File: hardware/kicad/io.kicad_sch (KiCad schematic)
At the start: 18 parts, among them J12 Conn_01x08, J15 Conn_01x02, J18 Conn_01x07, J4 UART_A, J5 UART_B, J6 Port_A, J7 Port_B, U11 74AC138, U12 SC16C752, U13 W65C22S

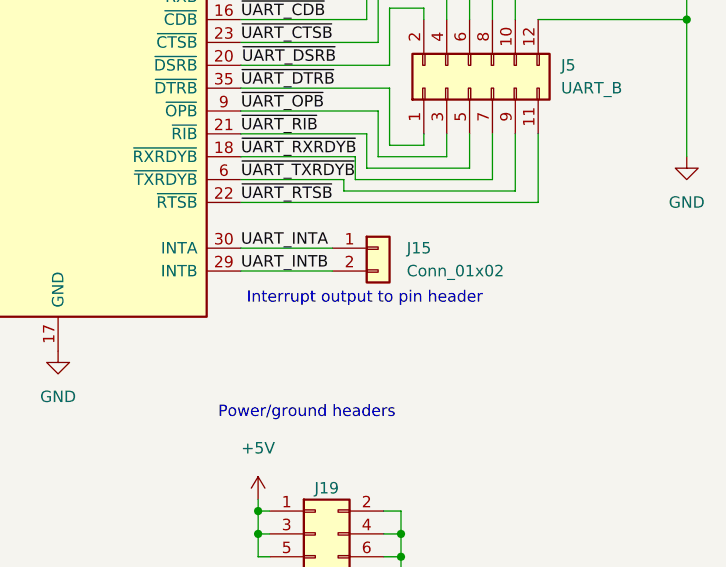
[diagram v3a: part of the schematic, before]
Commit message: add gerbers for test board
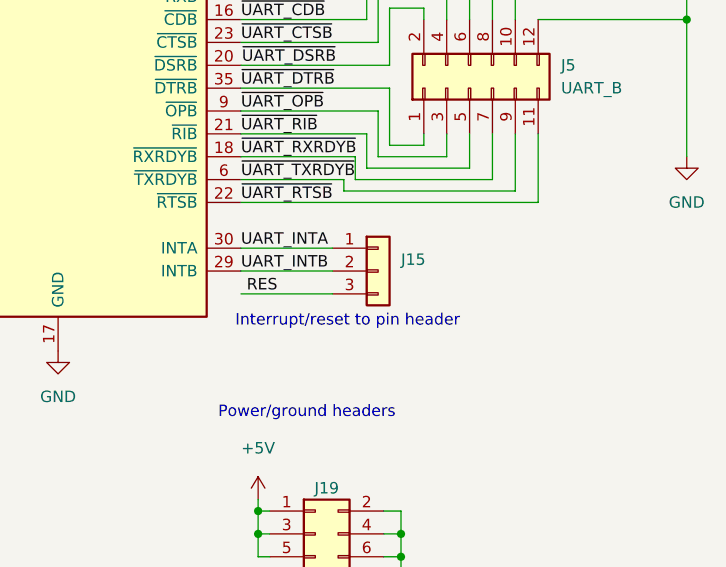
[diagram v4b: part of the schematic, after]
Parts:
- removed J15: Conn_01x02, Connector_PinHeader_2.54mm:PinHeader_1x02_P2.54mm_Vertical, symbol Connector_Generic:Conn_01x02
- added J15: (no value), symbol Connector_Generic:Conn_01x03
- J19: value (none) -> Conn_02x06; footprint (none) -> Connector_PinHeader_2.54mm:PinHeader_2x03_P2.54mm_Vertical
- J20: value (none) -> Conn_01x02; footprint (none) -> Connector_PinHeader_2.54mm:PinHeader_1x02_P2.54mm_Vertical
- J4: footprint Connector_PinHeader_2.54mm:PinHeader_2x06_P2.54mm_Vertical -> (none)
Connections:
- net RES: now also J15.3 (Pin_3)
- net UART_INTA: now also J15.1 (Pin_1)
- net UART_INTB: now also J15.2 (Pin_2)
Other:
- note added: "Interrupt/reset to pin header"
- note removed: "Interrupt output to pin header"
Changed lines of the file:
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@@
+    (stroke (width 0) (type default) (color 0 0 0 0))
+  )
+  (wire (pts (xy 223.52 100.33) (xy 233.68 100.33))
     (stroke (width 0) (type default) (color 0 0 0 0))
   )
@@
     (effects (font (size 1.27 1.27)) (justify left bottom))
   )
-  (text "Interrupt output to pin header" (at 224.155 101.6 0)
+  (text "Interrupt/reset to pin header" (at 222.885 104.14 0)
     (effects (font (size 1.27 1.27)) (justify left bottom))
   )
@@
   )
   (label "VIA_PB4" (at 91.44 154.94 0)
+    (effects (font (size 1.27 1.27)) (justify left bottom))
+  )
+  (label "RES" (at 224.155 100.33 0)
     (effects (font (size 1.27 1.27)) (justify left bottom))
   )
@@
     (in_bom yes) (on_board yes) (fields_autoplaced)
     (property "Reference" "J20" (id 0) (at 233.045 132.715 0))
-    (property "Value" "" (id 1) (at 233.045 132.08 0)
-      (effects (font (size 1.27 1.27)) hide)
-    )
-    (property "Footprint" "" (id 2) (at 233.045 139.065 0)
+    (property "Value" "Conn_01x02" (id 1) (at 233.045 132.08 0)
+      (effects (font (size 1.27 1.27)) hide)
+    )
+    (property "Footprint" "Connector_PinHeader_2.54mm:PinHeader_1x02_P2.54mm_Vertical" (id 2) (at 233.045 139.065 0)
       (effects (font (size 1.27 1.27)) hide)
     )
@@
     (pin "1")
   )
+  (symbol (lib_id "Connector_Generic:Conn_01x03") (at 238.76 97.79 0) (unit 1)
+    (in_bom yes) (on_board yes) (fields_autoplaced)
+    (property "Reference" "J15" (id 0) (at 241.3 96.5199 0)
+      (effects (font (size 1.27 1.27)) (justify left))
+    )
+    (property "Value" "" (id 1) (at 241.3 99.0599 0)
+      (effects (font (size 1.27 1.27)) (justify left))
+    )
+    (property "Footprint" "" (id 2) (at 238.76 97.79 0)
+      (effects (font (size 1.27 1.27)) hide)
+    )
+    (property "Datasheet" "~" (id 3) (at 238.76 97.79 0)
+      (effects (font (size 1.27 1.27)) hide)
+    )
+    (pin "1")
+    (pin "2")
+    (pin "3")
+  )
   (symbol (lib_id "Connector_Generic:Conn_02x06_Odd_Even") (at 105.41 120.65 0) (unit 1)
     (in_bom yes) (on_board yes) (fields_autoplaced)
@@
     (pin "1")
   )
-  (symbol (lib_id "Connector_Generic:Conn_01x02") (at 238.76 95.25 0) (unit 1)
-    (in_bom yes) (on_board yes) (fields_autoplaced)
-    (property "Reference" "J15" (id 0) (at 241.935 95.2499 0)
-      (effects (font (size 1.27 1.27)) (justify left))
-    )
-    (property "Value" "Conn_01x02" (id 1) (at 241.935 97.7899 0)
-      (effects (font (size 1.27 1.27)) (justify left))
-    )
-    (property "Footprint" "Connector_PinHeader_2.54mm:PinHeader_1x02_P2.54mm_Vertical" (id 2) (at 238.76 95.25 0)
-      (effects (font (size 1.27 1.27)) hide)
-    )
-    (property "Datasheet" "~" (id 3) (at 238.76 95.25 0)
-      (effects (font (size 1.27 1.27)) hide)
-    )
-    (pin "1")
-    (pin "2")
-  )
   (symbol (lib_id "Device:C") (at 129.54 179.07 0) (unit 1)
     (in_bom yes) (on_board yes)
@@
       (effects (font (size 1.27 1.27)) (justify right))
     )
-    (property "Footprint" "Connector_PinHeader_2.54mm:PinHeader_2x06_P2.54mm_Vertical" (id 2) (at 248.92 46.99 0)
+    (property "Footprint" "" (id 2) (at 248.92 46.99 0)
       (effects (font (size 1.27 1.27)) hide)
     )
@@
     (in_bom yes) (on_board yes)
     (property "Reference" "J19" (id 0) (at 233.045 121.92 0))
-    (property "Value" "" (id 1) (at 233.045 118.11 0)
-      (effects (font (size 1.27 1.27)) hide)
-    )
-    (property "Footprint" "" (id 2) (at 231.775 127 0)
-      (effects (font (size 1.27 1.27)) hide)
-    )
+    (property "Value" "Conn_02x06" (id 1) (at 233.045 118.11 0)
+      (effects (font (size 1.27 1.27)) hide)
+    )
+    (property "Footprint" "Connector_PinHeader_2.54mm:PinHeader_2x03_P2.54mm_Vertical" (id 2) (at 231.775 127 0)
+      (effects (font (size 1.27 1.27)) hide)
+    )
